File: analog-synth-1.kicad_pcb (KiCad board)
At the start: 2 copper layers, 56.6 x 106.5 mm, 55 parts, among them J1 CONN_02X08, J2 PJ301M-12, J3 PJ301M-12, J4 PJ301M-12, J5 PJ301M-12, Q1 2N3904, Q2 2N3904, Q3 2N3904, Q4 2N3906, Q5 2N3904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

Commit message: Finish PCB
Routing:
- net Sqr-SMPL: track 0.00 -> 120.4 mm
- net -12VA: track 32.3 -> 151.2 mm, vias 0 -> 3
- net +12V: track 39.2 -> 151.4 mm, vias 0 -> 1
- net Tri-SMPL: track 0.00 -> 65.3 mm
- net Net-(C9-Pad2): track 0.00 -> 52.3 mm, vias 0 -> 1
- net Net-(Q4-Pad2): track 0.00 -> 52.1 mm, vias 0 -> 1
- net Net-(Q2-Pad3): track 0.00 -> 43.8 mm, vias 0 -> 2
- net VIN: track 0.00 -> 41.7 mm
- net Exp-CV: track 0.00 -> 33.9 mm
- net Net-(C5-Pad2): track 3.83 -> 36.8 mm
- net Net-(R2-Pad1): track 0.00 -> 29.8 mm, vias 0 -> 1
- net Net-(J2-Pad2): track 0.00 -> 27.9 mm, vias 0 -> 1
- net CV: track 2.54 -> 29.7 mm, vias 0 -> 1
- net Triangle: track 0.00 -> 20.7 mm
- net Net-(C5-Pad1): track 3.81 -> 22.3 mm, vias 0 -> 1
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
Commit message: Fix VCO tuning rev1.0.13
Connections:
- R10 pad 2: Exp-CV -> Net-(R10-Pad2)
- R9 pad 2: Net-(R9-Pad2) -> Net-(R10-Pad2)
- RV4 pad 2: Net-(R9-Pad2) -> Net-(R10-Pad2)
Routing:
- net Net-(R10-Pad2): track 0.00 -> 15.7 mm
- net Net-(R9-Pad2): track 11.2 -> 0.00 mm
- net Exp-CV: track 33.9 -> 27.3 mm

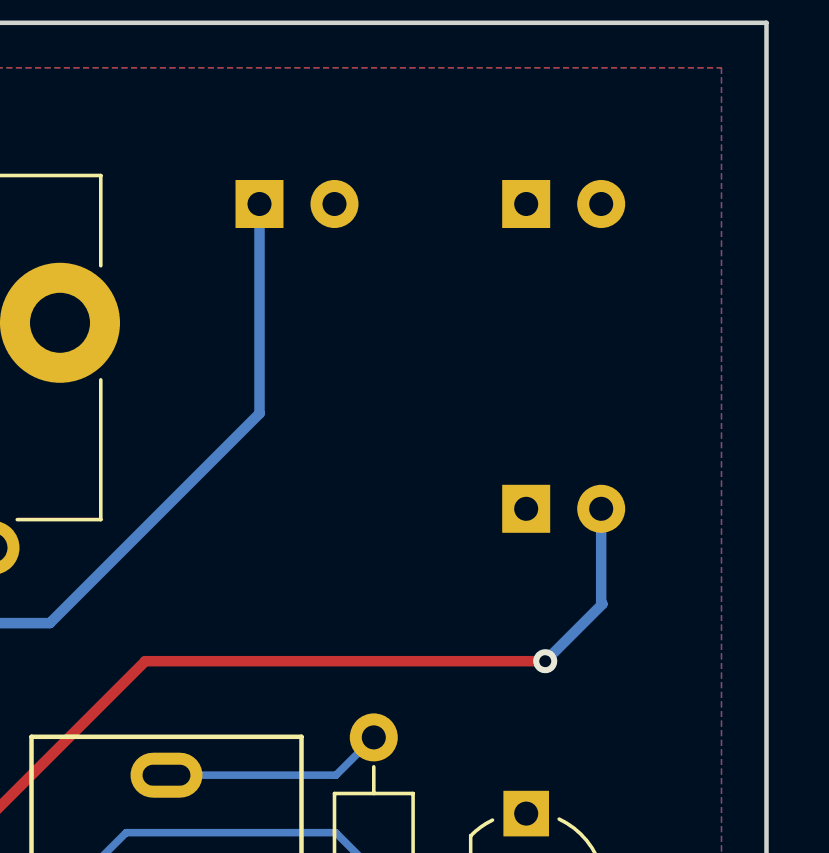
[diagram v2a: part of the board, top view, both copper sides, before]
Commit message: Fix polarized capacitor footprints rev1.0.14
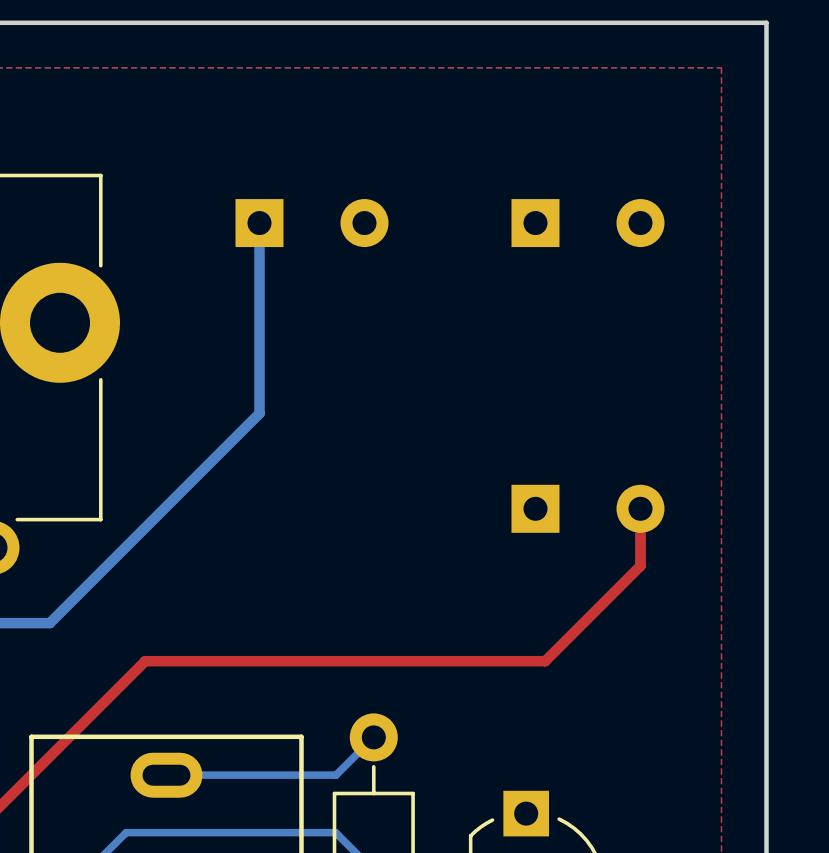
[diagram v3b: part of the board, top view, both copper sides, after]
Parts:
- C12, C13, C14: footprint Capacitors_THT:CP_Radial_D6.3mm_P2.50mm -> Capacitors_THT:CP_Radial_D8.0mm_P3.50mm
- moved C13 0.71 mm to (148.9, 66.7)
- moved C12 0.63 mm to (139.7, 66.7)
- moved C14 0.31 mm to (148.9, 76.2)
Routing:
- net +12V: track 151.4 -> 150.7 mm
- net -12VA: track 151.2 -> 151.7 mm, vias 3 -> 2
